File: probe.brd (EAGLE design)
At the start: 50.8 x 25.4 mm, 38 parts, among them U1 BMP180, U2 NX1117C33Z

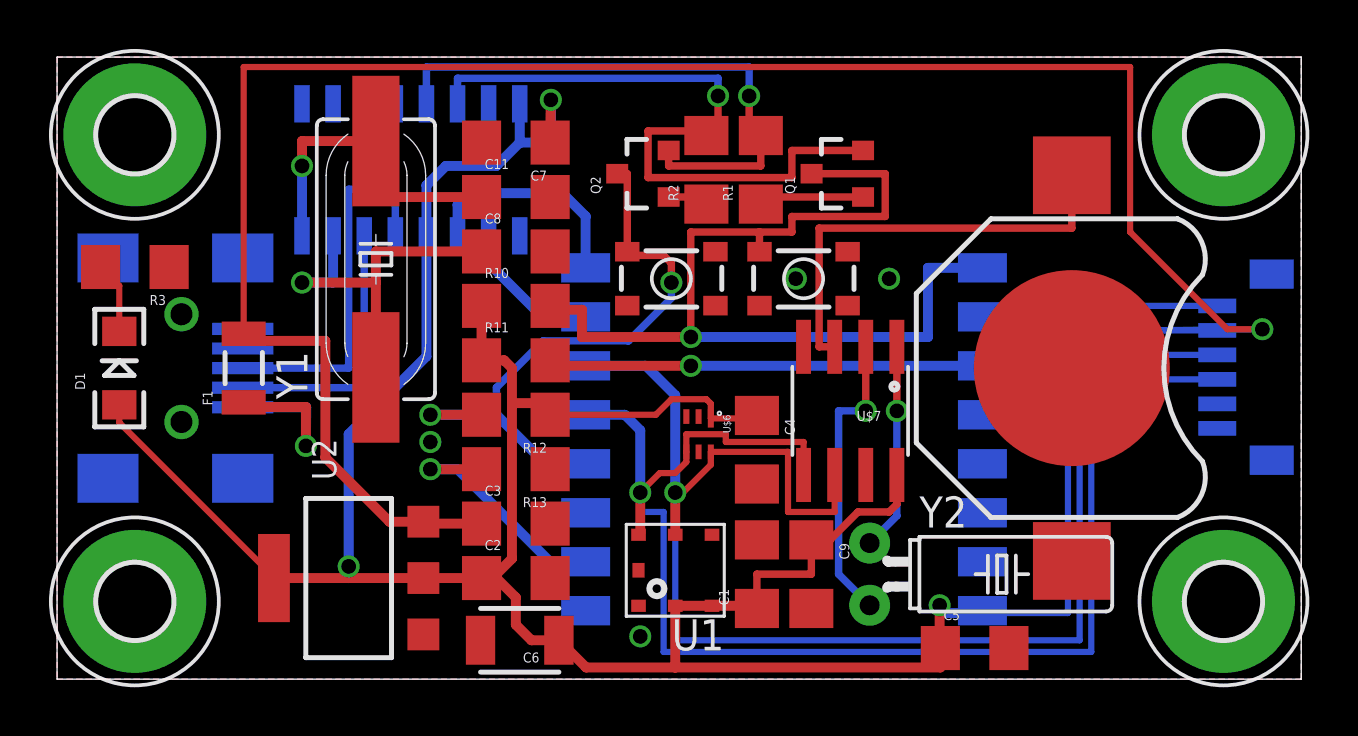
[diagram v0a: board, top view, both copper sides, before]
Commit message: Rounded corners
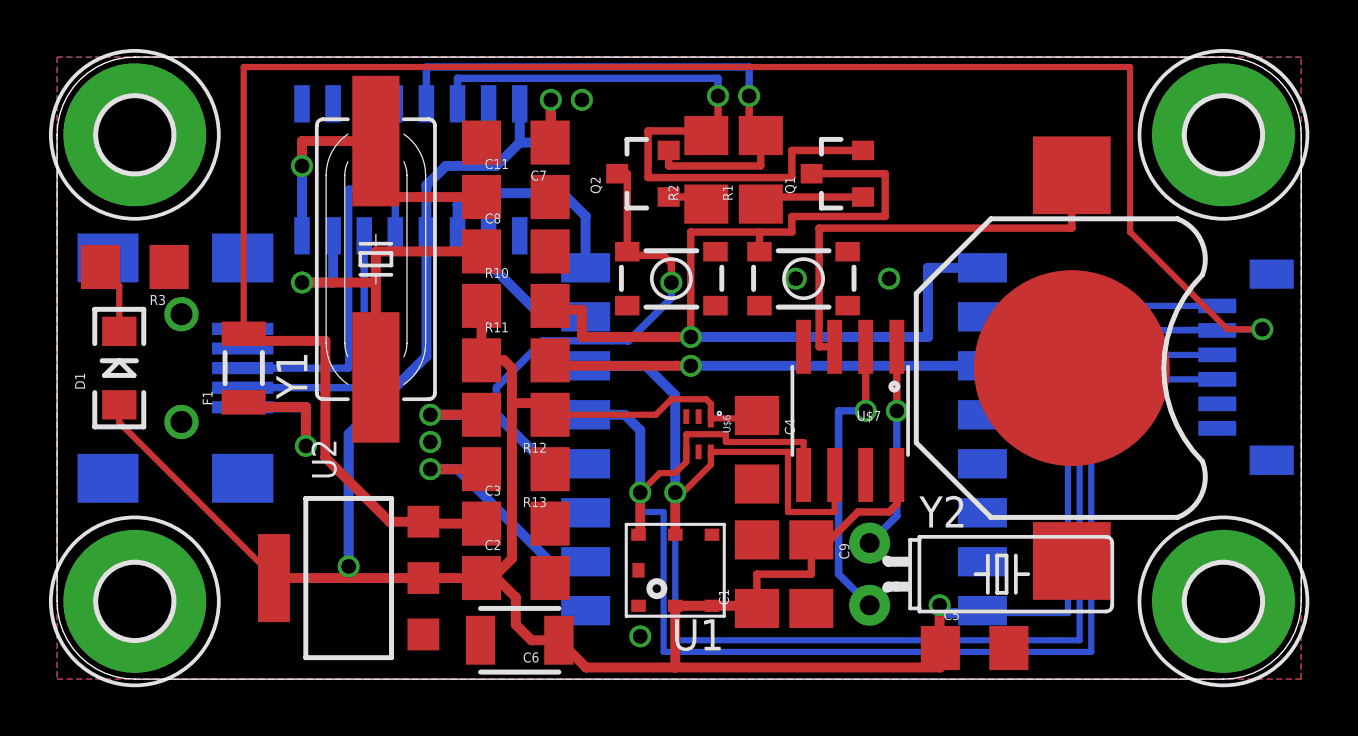
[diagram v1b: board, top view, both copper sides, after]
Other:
- outline, holes or cut-outs redrawn
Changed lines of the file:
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@@
 <board>
 <plain>
-<wire x1="0" y1="0" x2="50.8" y2="0" width="0" layer="20"/>
-<wire x1="50.8" y1="0" x2="50.8" y2="25.4" width="0" layer="20"/>
-<wire x1="50.8" y1="25.4" x2="0" y2="25.4" width="0" layer="20"/>
-<wire x1="0" y1="25.4" x2="0" y2="0" width="0" layer="20"/>
+<wire x1="3.175" y1="0" x2="47.625" y2="0" width="0" layer="20"/>
+<wire x1="47.625" y1="0" x2="50.8" y2="3.175" width="0" layer="20" curve="90"/>
+<wire x1="50.8" y1="3.175" x2="50.8" y2="22.225" width="0" layer="20"/>
+<wire x1="50.8" y1="22.225" x2="47.625" y2="25.4" width="0" layer="20" curve="90"/>
+<wire x1="47.625" y1="25.4" x2="3.175" y2="25.4" width="0" layer="20"/>
+<wire x1="3.175" y1="25.4" x2="0" y2="22.225" width="0" layer="20" curve="90"/>
+<wire x1="0" y1="22.225" x2="0" y2="3.175" width="0" layer="20"/>
+<wire x1="0" y1="3.175" x2="3.175" y2="0" width="0" layer="20" curve="90"/>
 </plain>
 <attributes>
@@
 <contactref element="JP1" pad="5"/>
 <contactref element="R3" pad="1"/>
-<wire x1="20.1325" y1="17.4625" x2="18.89125" y2="18.10125" width="0" layer="19" extent="1-16"/>
+<via x="21.43125" y="23.65375" extent="1-16" drill="0.6" shape="square"/>
 </signal>
 <signal name="GPIO2">
